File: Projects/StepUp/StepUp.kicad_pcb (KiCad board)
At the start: 4 copper layers, 50 x 80 mm, 152 parts, among them J1 USB_C_Receptacle_USB2.0_16P, J2 Conn_02x03_Odd_Even, J4 AST250404, Q1 BSS84, Q2 2N7002-7-F, Q3 PMF170XP,115, Q4 2N7002-7-F, Q5 SSM3J328R_LF, Q6 2N7002-7-F, Q7 2N7002-7-F, SW1 PTS636SL43SMTRLFS, SW2 PTS636SL43SMTRLFS, SW3 1825027-8, U1 W25Q16JVUXIQ TR, U2 USBLC6-2SC6, U3 RP2040, U4 TMC2300-LA, U5 LDL1117S33R, U6 MCP73832T-2ACI_OT, U7 MIC2253, U8 ECH8697R-TL-W, U9 BQ297xy, Y1 ABM8-272-T3

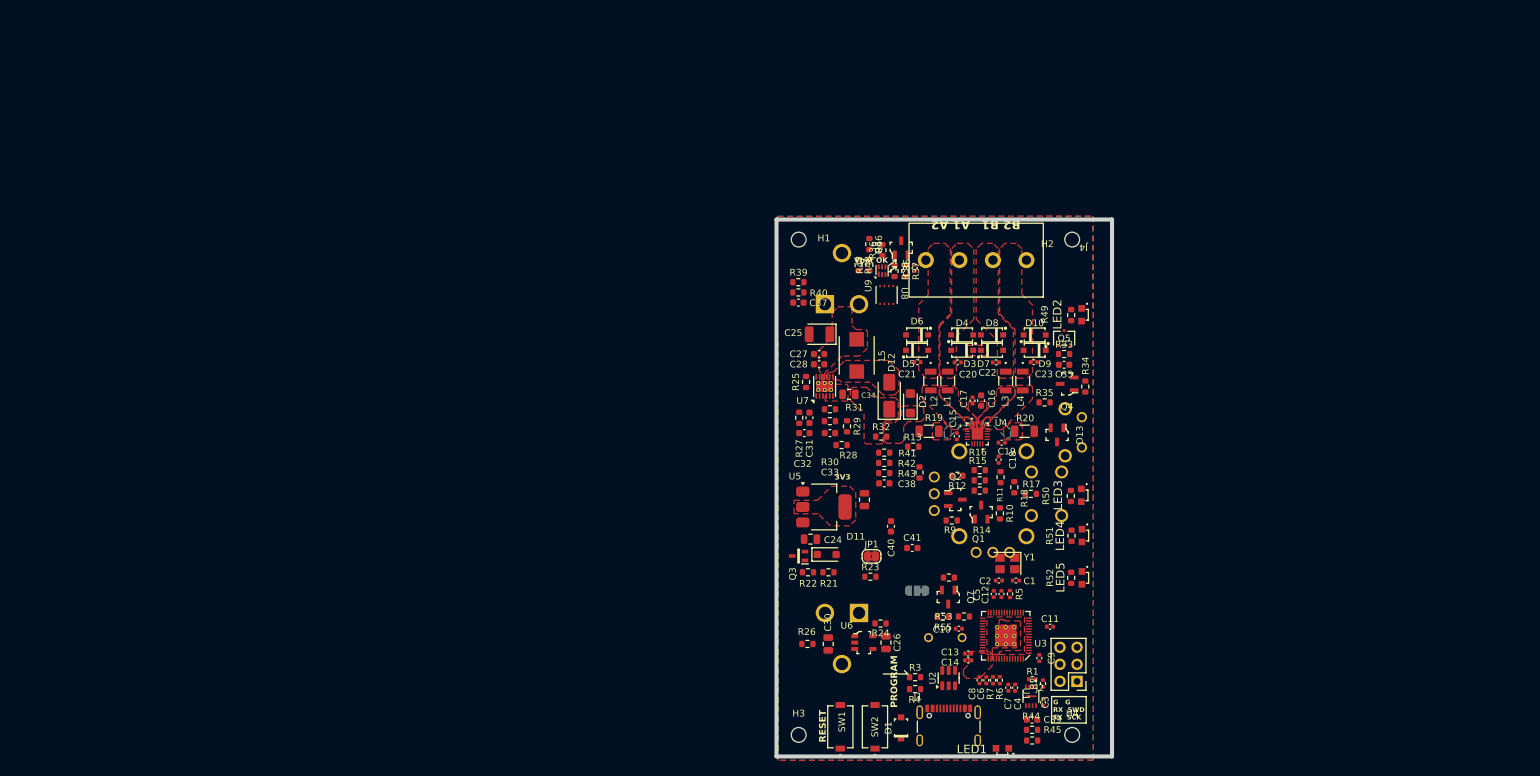
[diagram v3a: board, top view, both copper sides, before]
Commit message: feat(v0.2): Component layout from CAD
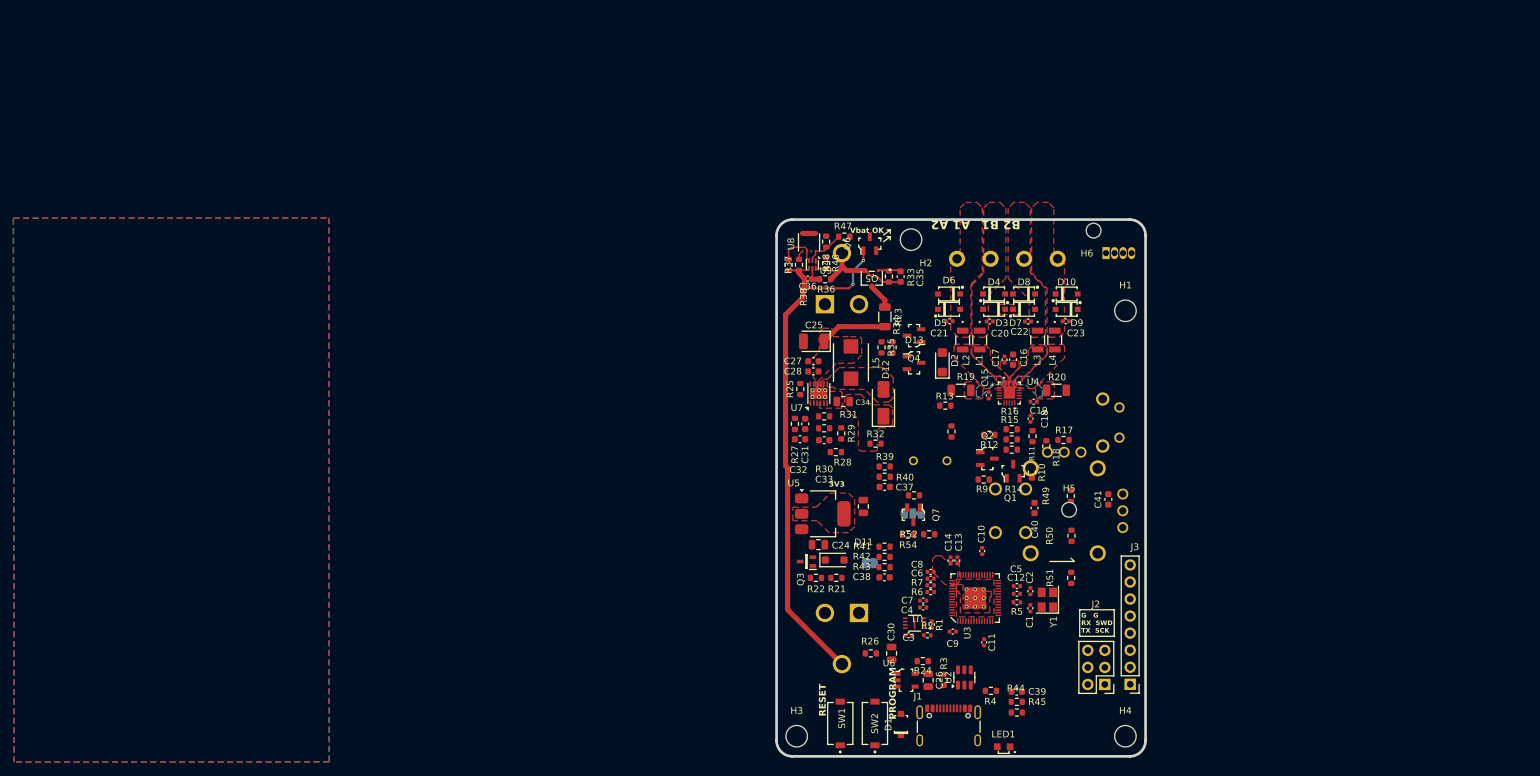
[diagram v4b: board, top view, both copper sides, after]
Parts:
- removed LED2: IN-S63ASR, Samacsys:LEDC1706X110N
- removed LED3, LED4, LED5: IN-S63AS5UW, Samacsys:INS63AS5UW
- removed the R49 at (100.3, 64.3)
- added D14: LED_ARGB, LED_THT:LED_D5.0mm-4_RGB, B.Cu at (105.5, 55.1)
- added H5: MountingHole, MountingHole:MountingHole_2.2mm_M2, F.Cu at (100.0, 93.3)
- added H6: MountingHole, MountingHole:MountingHole_2.2mm_M2, F.Cu at (103.7, 51.8)
- added J3: Conn_01x08_Pin, Connector_PinHeader_2.54mm:PinHeader_1x08_P2.54mm_Vertical, F.Cu at (109.1, 119.3)
- H1, H2, H3, H4: footprint MountingHole:MountingHole_2.2mm_M2 -> MountingHole:MountingHole_3.2mm_M3_DIN965
- J4, JP1: moved to B.Cu
- R23: footprint Resistor_SMD:R_0603_1608Metric -> Resistor_SMD:R_1206_3216Metric
- U9: value BQ297xy -> BQ2970
- moved H1 49.8 mm to (108.4, 63.7)
- moved R23 38.8 mm to (72.5, 64.6), turned to 90 degrees
- moved R39 30.3 mm to (72.5, 86.9)
- moved R40 30.3 mm to (72.5, 88.4)
- moved C37 30.3 mm to (72.5, 89.9)
- moved C41 30.1 mm to (105.8, 91.8), turned to -90 degrees
- moved Q5 30.0 mm to (70.6, 58.9), turned to 180 degrees
- moved R34 29.3 mm to (73.7, 69.2)
- moved R33 28.5 mm to (73.2, 58.6), turned to -90 degrees
- moved JOY1 28.2 mm to (108.0, 91.0), turned to 90 degrees
- moved C35 27.7 mm to (74.9, 58.6), turned to 90 degrees
- moved BZ1 26.4 mm to (79.3, 86.0)
- moved R35 25.6 mm to (72.0, 69.2), turned to -90 degrees
- moved H2 24.0 mm to (76.5, 53.1)
- moved Q4 23.9 mm to (76.9, 67.4)
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- renumbered R50 to R49, R51 to R50, R52 to R51, R53 to R52, R54 to R53, R55 to R54
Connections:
- C20 pad 2: OA1_OUT -> /Motor Driver/OA1_OUT
- C21 pad 1: OA2_OUT -> /Motor Driver/OA2_OUT
- C22 pad 2: OB1_OUT -> /Motor Driver/OB1_OUT
- C23 pad 1: OB2_OUT -> /Motor Driver/OB2_OUT
- D10 pad 1: OB2_OUT -> /Motor Driver/OB2_OUT
- D3 pad 2: OA1_OUT -> /Motor Driver/OA1_OUT
- D4 pad 1: OA1_OUT -> /Motor Driver/OA1_OUT
- D5 pad 2: OA2_OUT -> /Motor Driver/OA2_OUT
- D6 pad 1: OA2_OUT -> /Motor Driver/OA2_OUT
- D7 pad 2: OB1_OUT -> /Motor Driver/OB1_OUT
- D8 pad 1: OB1_OUT -> /Motor Driver/OB1_OUT
- D9 pad 2: OB2_OUT -> /Motor Driver/OB2_OUT
- J4 pad 1: (no net) -> /Motor Driver/OA1_OUT
- J4 pad 2: (no net) -> /Motor Driver/OA2_OUT
- J4 pad 3: (no net) -> /Motor Driver/OB1_OUT
- J4 pad 4: (no net) -> /Motor Driver/OB2_OUT
- L1 pad 1: OA1_OUT -> /Motor Driver/OA1_OUT
- L2 pad 1: OA2_OUT -> /Motor Driver/OA2_OUT
- L3 pad 1: OB1_OUT -> /Motor Driver/OB1_OUT
- L4 pad 1: OB2_OUT -> /Motor Driver/OB2_OUT
- U3 pad 4: MCU_LED_ERROR -> /MCU/GPIO2
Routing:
- net /Power/VBAT_PACK_NEG: track 0.00 -> 79.9 mm, vias 0 -> 2
- net /Power/VBAT_PACK_POS: track 0.00 -> 14.5 mm
- net BOOST_VIN: track 0.00 -> 9.97 mm
- net Net-(U8-G1): track 0.00 -> 6.23 mm
- net Net-(U8-G2): track 0.00 -> 5.95 mm
- net Vbat: track 0.00 -> 3.95 mm
- net Net-(Q4-D): track 0.00 -> 3.45 mm
- net Net-(U9-BAT): track 0.00 -> 2.95 mm
- net Net-(U8-D-Pad5): track 0.00 -> 1.95 mm
- net Net-(U9-V-): track 0.00 -> 1.57 mm
- net Net-(U8-S1): track 0.00 -> 1.42 mm
- added copper zone on F.Cu, net /Motor Driver/OA1_OUT
- added copper zone on F.Cu, net /Motor Driver/OA2_OUT
- added copper zone on F.Cu, net /Motor Driver/OB1_OUT
- added copper zone on F.Cu, net /Motor Driver/OB2_OUT
- removed copper zone on F.Cu, net OA1_OUT
- removed copper zone on F.Cu, net OA2_OUT
- removed copper zone on F.Cu, net OB1_OUT
- removed copper zone on F.Cu, net OB2_OUT
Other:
- board size 50 x 80 mm -> 55 x 80 mm

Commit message: feat(layout): Layout begins
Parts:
- J2, J3: moved to B.Cu
- moved R51 34.2 mm to (105.4, 69.6)
- moved R50 29.1 mm to (109.8, 69.8)
- moved R26 23.3 mm to (90.3, 126.8)
- moved R49 23.0 mm to (107.9, 69.6)
- moved R10 8.81 mm to (85.9, 89.9)
- moved C40 7.51 mm to (99.4, 87.1), turned to 0 degrees
- moved R54 4.26 mm to (79.3, 94.3)
- moved R52 4.26 mm to (82.5, 94.3)
- moved R53 4.26 mm to (80.2, 88.5)
- moved Q7 4.26 mm to (80.1, 91.4)
- moved D13 4.20 mm to (76.9, 67.2)
- moved Q4 4.20 mm to (76.9, 63.2), turned to 0 degrees
- moved R12 4.10 mm to (86.1, 78.6)
- moved Q2 4.10 mm to (85.8, 82.2)
- moved R24 4.09 mm to (74.1, 115.5)
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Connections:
- BT1 pad 1: GND -> /Power/VBAT_PACK_POS
- BT1 pad 2: GND -> /Power/VBAT_PACK_POS
- BT2 pad 1: GND -> /Power/VBAT_PACK_NEG
- BT2 pad 2: GND -> /Power/VBAT_PACK_NEG
- J4 pad 1: /Motor Driver/OA1_OUT -> /Motor Driver/OA2_OUT
- J4 pad 2: /Motor Driver/OA2_OUT -> /Motor Driver/OA1_OUT
- JOY1 pad 11: GND -> +3V3
- JOY1 pad 13: +3V3 -> GND
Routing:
- net +3V3: track 0.00 -> 25.9 mm
- net Net-(Q4-D): track 3.45 -> 14.6 mm
- net /MCU/XIN: track 0.00 -> 9.45 mm
- net /Motor Driver/TMC_VCC_IO: track 0.00 -> 9.10 mm
- net BOOST_VOUT: track 0.00 -> 8.81 mm
- net Net-(Q4-G): track 0.00 -> 7.23 mm
- net TMC_UART_RX: track 0.00 -> 7.00 mm
- net Net-(D11-K): track 0.00 -> 6.88 mm
- net Net-(U7-COMP): track 0.00 -> 6.08 mm
- net +1V1: track 0.00 -> 5.96 mm
- net Net-(U7-FB): track 0.00 -> 5.64 mm
- net Net-(C2-Pad1): track 0.00 -> 3.80 mm
- net MCU_BOOST_EN: track 0.00 -> 3.30 mm
- net Net-(U7-SS): track 0.00 -> 2.85 mm
- net Net-(U4-1.8VOUT): track 0.00 -> 2.68 mm
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- added copper zone on F.Cu, net /Power/VBAT_PACK_NEG
- added copper zone on F.Cu, net /Power/VBAT_PACK_POS
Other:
- board text removed: "Vbat OK"

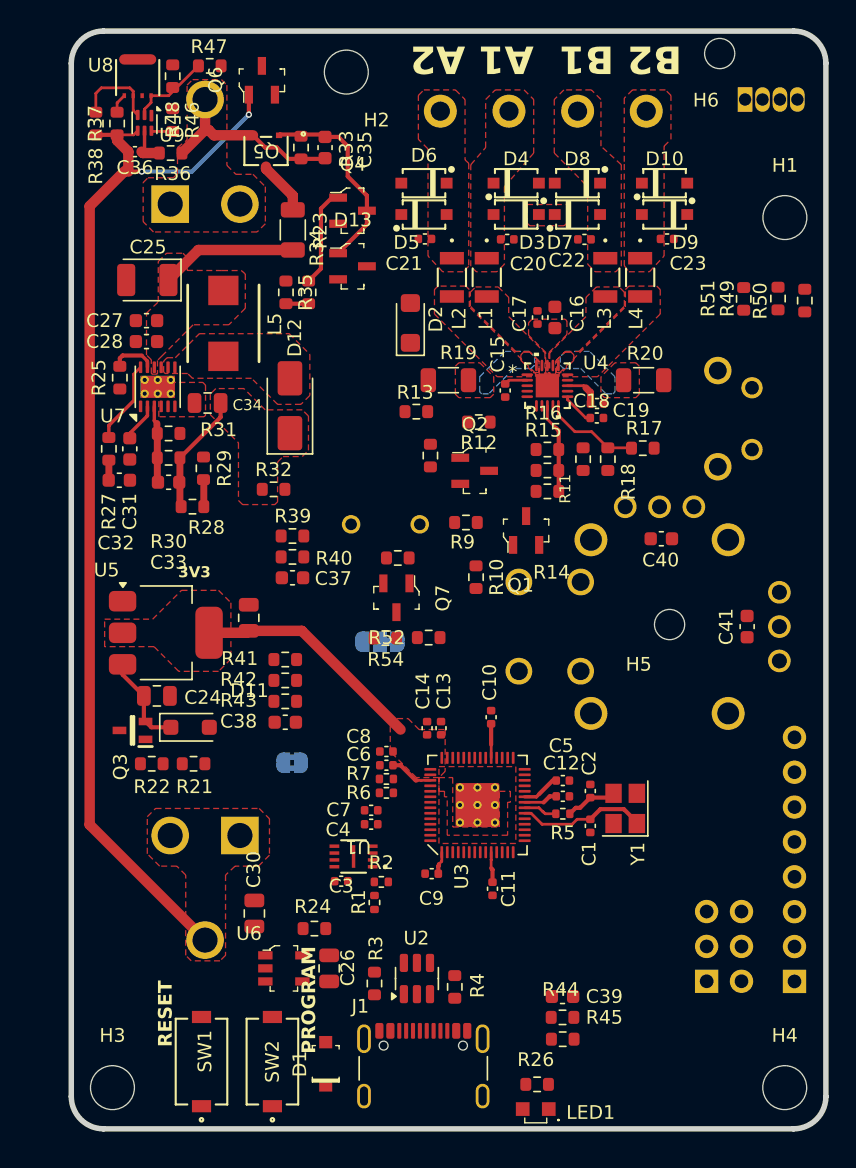
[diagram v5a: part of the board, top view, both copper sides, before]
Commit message: feat(layout): Most traces complete
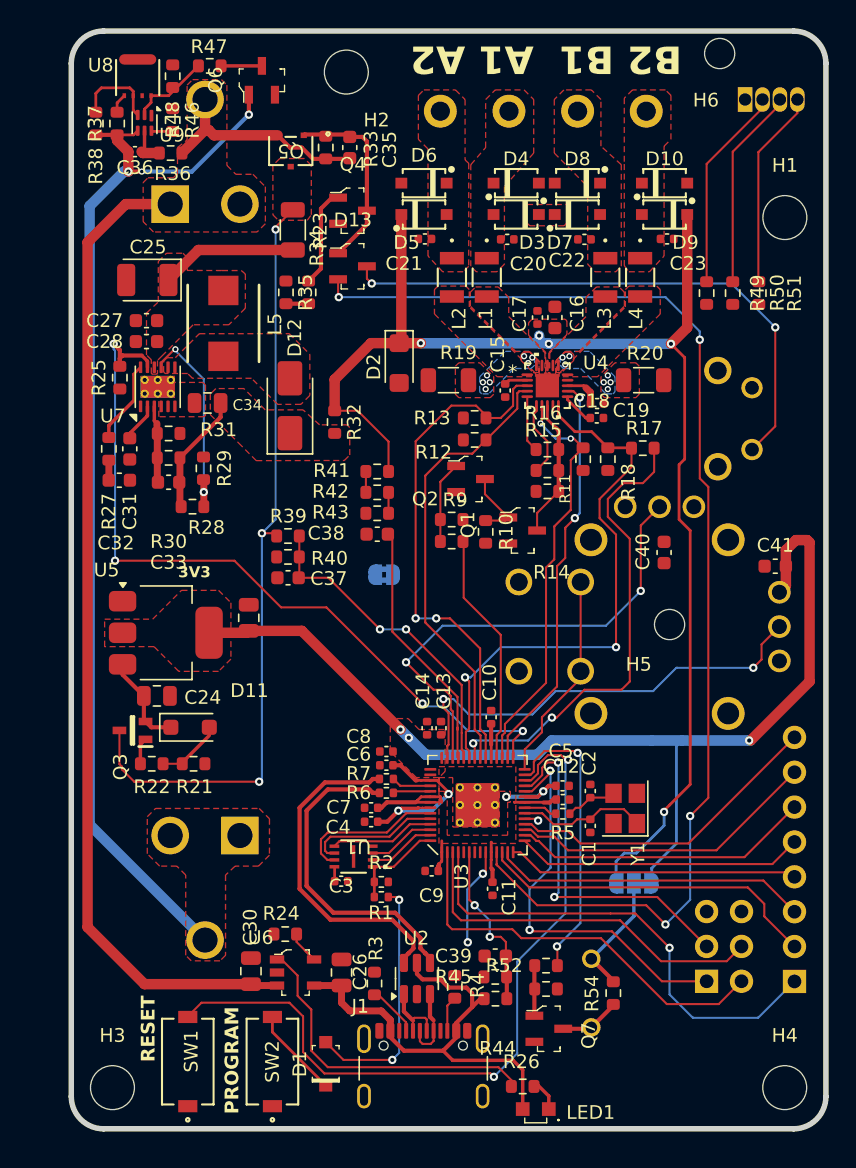
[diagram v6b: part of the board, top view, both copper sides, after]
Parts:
- moved BZ1 37.3 mm to (94.3, 120.2), turned to 0 degrees
- moved Q7 33.3 mm to (91.2, 122.8), turned to 0 degrees
- moved R53 33.2 mm to (91.0, 119.9), turned to 180 degrees
- moved R54 30.7 mm to (95.9, 120.2), turned to 90 degrees
- moved JP2 25.5 mm to (97.4, 112.2)
- moved R52 25.4 mm to (91.0, 118.2)
- moved C38 15.3 mm to (78.7, 86.8)
- moved JP1 15.3 mm to (79.2, 89.7)
- moved R41 15.3 mm to (78.7, 82.2)
- moved R42 15.3 mm to (78.7, 83.7)
- moved R43 15.3 mm to (78.7, 85.2)
- moved R32 6.62 mm to (75.6, 78.6), turned to -90 degrees
- moved R8 6.45 mm to (84.1, 87.3), turned to 180 degrees
- moved C39 5.72 mm to (87.3, 117.5), turned to 0 degrees
- moved R45 5.72 mm to (87.3, 119.0), turned to 0 degrees
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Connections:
- C30 pad 1: Vbat -> /Power/VBAT_PACK_POS
- U6 pad 3: Vbat -> /Power/VBAT_PACK_POS
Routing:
- net VMotor: track 0.00 -> 97.8 mm, vias 0 -> 5
- net MCU_PWR_BTN: track 0.00 -> 88.5 mm, vias 0 -> 4
- net /Power/VBAT_PACK_POS: track 14.5 -> 88.9 mm
- net +3V3: track 25.9 -> 96.0 mm, vias 0 -> 3
- net /MCU/RUN: track 0.00 -> 56.3 mm, vias 0 -> 2
- net MCU_BOOST_EN: track 3.30 -> 58.1 mm, vias 0 -> 4
- net Vbat: track 3.95 -> 57.1 mm, vias 0 -> 3
- net Net-(D13-Pad3): track 0.00 -> 41.7 mm, vias 0 -> 2
- net TMC_DIR: track 0.00 -> 38.0 mm, vias 0 -> 2
- net JOY_AXIS_MCU_V: track 0.00 -> 34.8 mm, vias 0 -> 2
- net /MCU/GPIO2: track 0.00 -> 34.8 mm, vias 0 -> 1
- net TMC_UART_TX: track 0.00 -> 34.3 mm, vias 0 -> 2
- net TMC_UART_RX: track 7.00 -> 41.1 mm, vias 0 -> 2
- net V_USB: track 0.00 -> 33.7 mm
- net TMC_STEP: track 0.00 -> 32.9 mm
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- added copper zone on F.Cu, net Vbat

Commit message: feat(v0.2): Release, PCBs ordered!
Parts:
- removed the D14 at (105.5, 55.1)
- removed J3: Conn_01x08_Pin, Connector_PinHeader_2.54mm:PinHeader_1x08_P2.54mm_Vertical
- added D15: LED_ARGB, LED_THT:LED_D5.0mm-4_RGB_Staggered_Pins, B.Cu at (106.9, 52.9)
- added FID1: Fiducial, Fiducial:Fiducial_1mm_Mask2mm, F.Cu at (58.5, 120.5)
- added FID2: Fiducial, Fiducial:Fiducial_1mm_Mask2mm, F.Cu at (79.8, 55.8)
- added FID3: Fiducial, Fiducial:Fiducial_1mm_Mask2mm, F.Cu at (108.5, 83.3)
- added J5: Conn_01x09_Pin, Connector_PinHeader_2.54mm:PinHeader_1x09_P2.54mm_Vertical, B.Cu at (109.1, 122.0)
- added J6: Conn_01x05, Connector_PinHeader_2.54mm:PinHeader_1x05_P2.54mm_Vertical, B.Cu at (94.6, 128.2)
- C35: footprint Capacitor_SMD:C_0603_1608Metric -> Capacitor_SMD:C_0805_2012Metric
- J4: value AST250404 -> AST0250404
- R24: value 2.7kR -> 2.49kR
- SW1, SW2: value PTS636SL43SMTRLFS -> PTS636SP43SMTRL FS
- U4: value TMC2300-LA -> TMC2300-LA-T
- moved JP1 13.1 mm to (72.3, 100.9), turned to 0 degrees
- moved C40 1.82 mm to (98.0, 87.2)
- moved Y1 1.06 mm to (96.6, 105.7)
- moved C11 0.50 mm to (87.4, 112.2)
- moved D14 0.47 mm to (76.9, 67.7)
- moved C9 0.38 mm to (82.3, 111.2)
- moved C2 0.36 mm to (94.0, 105.2)
- moved R24 0.33 mm to (72.3, 116.0)
- moved C1 0.22 mm to (94.1, 108.2)
- moved C35 0.13 mm to (76.8, 58.5)
- renumbered LED1 to D12, D12 to D13, D13 to D14
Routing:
- net +3V3: track 96.0 -> 230.5 mm, vias 3 -> 9
- net MCU_LED_STATUS_3: track 0.00 -> 70.6 mm, vias 0 -> 2
- net MCU_LED_STATUS_2: track 0.00 -> 69.6 mm, vias 0 -> 2
- net MCU_LED_STATUS_1: track 0.00 -> 68.5 mm, vias 0 -> 2
- net MCU_PWR_CTRL: track 8.78 -> 66.1 mm, vias 2 -> 4
- net Vbat: track 57.1 -> 109.5 mm, vias 3 -> 4
- net VMotor: track 97.8 -> 141.2 mm, vias 5 -> 8
- net V_USB: track 33.7 -> 65.9 mm, vias 0 -> 1
- net GND: track 1.04 -> 8.82 mm, vias 1 -> 87
- net Net-(D11-A): track 4.87 -> 12.6 mm, vias 0 -> 1
- net /MCU/SWD: track 26.0 -> 29.6 mm
- net VMOTOR_MONITOR: track 20.1 -> 23.6 mm
- net Net-(D15-RK): track 15.0 -> 18.0 mm
- net Net-(D15-BK): track 14.5 -> 12.0 mm
- net /Motor Driver/TMC_VCC_IO: track 12.9 -> 15.0 mm, vias 0 -> 2
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- added copper zone on B.Cu, net /Power/VBAT_PACK_NEG
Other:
- board text added: "0.2000 mm"
- board text added: "54.9766 mm x 79.9766 mm"
- board text added: "@SJFOM"
- board text added: "E"
- board text added: "GP15 GP14 GP13 GP12 GP11 GP10 GP9 GP2 GND"
- board text added: "P"
- board text added: "S"
- board text added: "T"
- board text added: "UP!"
- board text added: "Vusb Vbat Vmot 3v3 GND"
- board text added: "v0.2"
- board text removed: "0.3000 mm"
- board text removed: "47.0223 mm x 81.0223 mm"
- board text removed: "SJFOM"
- board text removed: "StepUp! v0.2"

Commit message: feat(v0.3): Begin work on next rev
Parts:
- removed JP1: SolderJumper_2_Bridged, Jumper:SolderJumper-2_P1.3mm_Bridged2Bar_RoundedPad1.0x1.5mm
- removed JP2: SolderJumper_3_Bridged12, Jumper:SolderJumper-3_P1.3mm_Bridged12_RoundedPad1.0x1.5mm
- added BT3: 54, Samacsys:54, F.Cu at (26.2, 110.5)
- added C36: 10uF, Capacitor_SMD:C_0805_2012Metric, F.Cu at (32.5, 118.8)
- added LED1: MP008267, Samacsys:MP008267, B.Cu at (108.4, 57.2)
- added R36: 10kR, Resistor_SMD:R_0603_1608Metric, F.Cu at (36.7, 118.5)
- added R56: 120R, Resistor_SMD:R_0603_1608Metric, F.Cu at (113.8, 61.7)
- D15: value LED_ARGB -> 1N4148W-TP; footprint LED_THT:LED_D5.0mm-4_RGB_Staggered_Pins -> digikey-footprints:SOD-123; moved to F.Cu
- R50: renamed from R49; value 100R -> 120R
- R51: value 100R -> 120R
- R52: renamed from R50; value 100R -> 22R
- moved D15 103.9 mm to (26.6, 118.9), turned to 0 degrees
- moved H6 45.8 mm to (78.0, 89.6)
- moved R51 12.3 mm to (113.8, 59.2), turned to 0 degrees
- moved SW3 5.00 mm to (111.9, 73.3)
- moved R50 1.15 mm to (102.7, 68.0)
- moved R52 1.15 mm to (104.6, 68.0)
- renumbered C36 to C37, C37 to C38, C38 to C39, C39 to C40, C40 to C41, C41 to C42, J5 to J2, J2 to J3, J6 to J5, R36 to R37, R37 to R38, R38 to R39, R39 to R40, R40 to R41, R41 to R42, R42 to R43, R43 to R44, R44 to R45, R45 to R46, R46 to R47, R47 to R48, R48 to R49, R52 to R53, R53 to R54, R54 to R55
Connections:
- net MCU_LED_STATUS_1 renamed MCU_LED_RED
- net MCU_LED_STATUS_3 renamed MCU_LED_GREEN
- BZ1 pad 2: Net-(JP2-C) -> VMotor
- D11 pad 2: Net-(D11-A) -> V_USB
- R21 pad 2: Net-(D11-A) -> V_USB
- R22 pad 1: Net-(D11-A) -> V_USB
- R50 pad 1: Net-(D15-RK) -> Net-(LED1-Pad1)
- R51 pad 1: Net-(D15-BK) -> Net-(LED1-Pad4)
- R52 pad 1: Net-(D15-GK) -> Net-(LED1-Pad3)
- R55 pad 2: Net-(JP2-C) -> VMotor
- U3 pad 7: MCU_LED_STATUS_2 -> MCU_LED_BLUE
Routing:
- net MCU_LED_STATUS_2: track 69.6 -> 0.00 mm, vias 2 -> 0
- net MCU_LED_BLUE: track 0.00 -> 58.1 mm, vias 0 -> 2
- net +3V3: track 230.5 -> 190.5 mm
- net Net-(LED1-Pad1): track 0.00 -> 30.1 mm
- net Net-(D15-RK): track 18.0 -> 0.00 mm
- net MCU_LED_RED: track 68.5 -> 53.4 mm
- net Net-(D14-Pad3): track 42.1 -> 27.2 mm, vias 2 -> 1
- net Net-(LED1-Pad3): track 0.00 -> 14.0 mm
- net Net-(D15-GK): track 14.0 -> 0.00 mm
- net V_USB: track 65.9 -> 78.5 mm, vias 1 -> 2
- net Net-(D11-A): track 12.6 -> 0.00 mm, vias 1 -> 0
- net MCU_LED_GREEN: track 70.6 -> 58.1 mm
- net Net-(D15-BK): track 12.0 -> 0.00 mm
- net VMotor: track 141.2 -> 150.3 mm
- net Net-(JP2-C): track 9.12 -> 0.00 mm
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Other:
- board text added: "GND 3v3 Vmot Vbat Vusb"
- board text added: "v0.3"
- board text removed: "Vusb Vbat Vmot 3v3 GND"
- board text removed: "v0.2"
